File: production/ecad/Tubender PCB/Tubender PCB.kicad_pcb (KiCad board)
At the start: 2 copper layers, 210 parts, among them J10 640387-5, J11 640387-8, J12 640387-2, J13 640387-5, J14 640387-3, J15 640387-2, J16 640387-2, J17 640387-2, J18 640387-2, J19 640387-2, J2 640387-5, J20 640387-2, J21 640387-2, J22 640387-2, J23 640387-2, J24 640387-2, J25 640387-2, J26 640387-2, J27 640387-2, J28 640387-2, J29 1-640387-0, J3 640387-5, J30 640387-2, J31 640387-5, J32 USB4110GFA, J4 640387-5, J5 640387-6, J6 640387-6, J8 640387-6, J9 640387-5, Q1 AO3400A, Q2 AO3400A, U1 LMR36520FADDAR, U10 MCP23017-E_SO, U11 SN74AHC1G125DBVR, U12 LM5146RGYR, U13 LM5017SDX/NOPB, U2 ESP32-WROOM-32UE_M113EH6400UH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, U3 MCP23017-E_SO, U5 TPSM265R1V5SILR, U6 CP2102N-A02-GQFN28, U8 CD4051BE, U9 CD4051BE, Y1 ABM8-20.000MHz-10-B1U-T

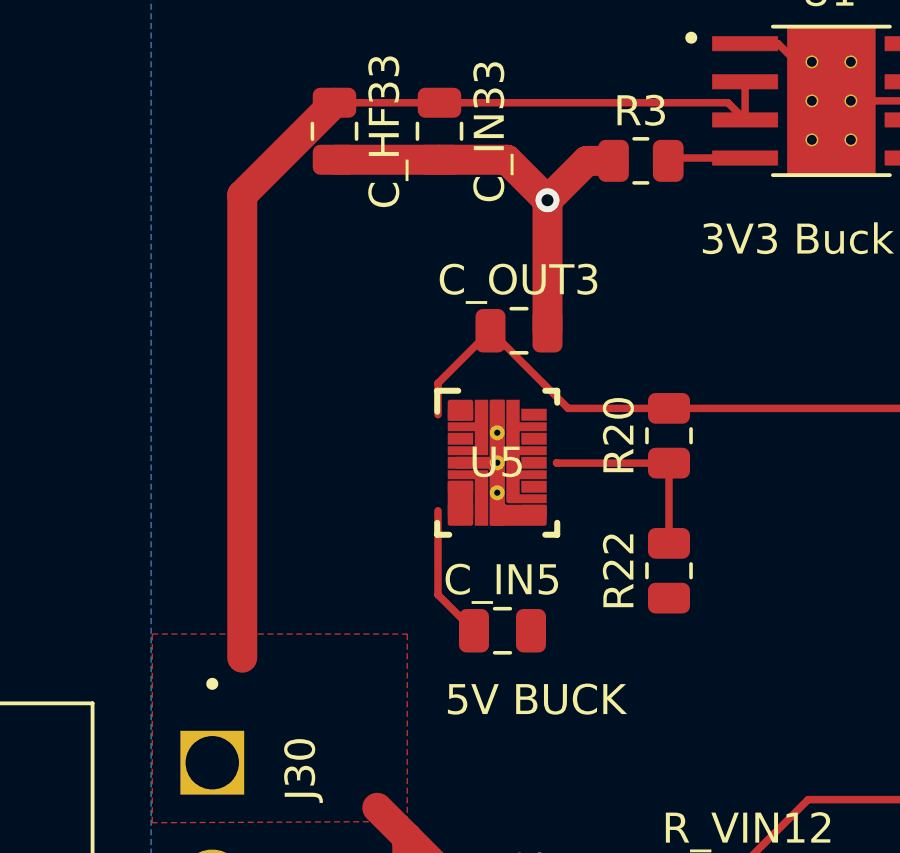
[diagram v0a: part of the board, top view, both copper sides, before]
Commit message: connected one line on 5V Buck
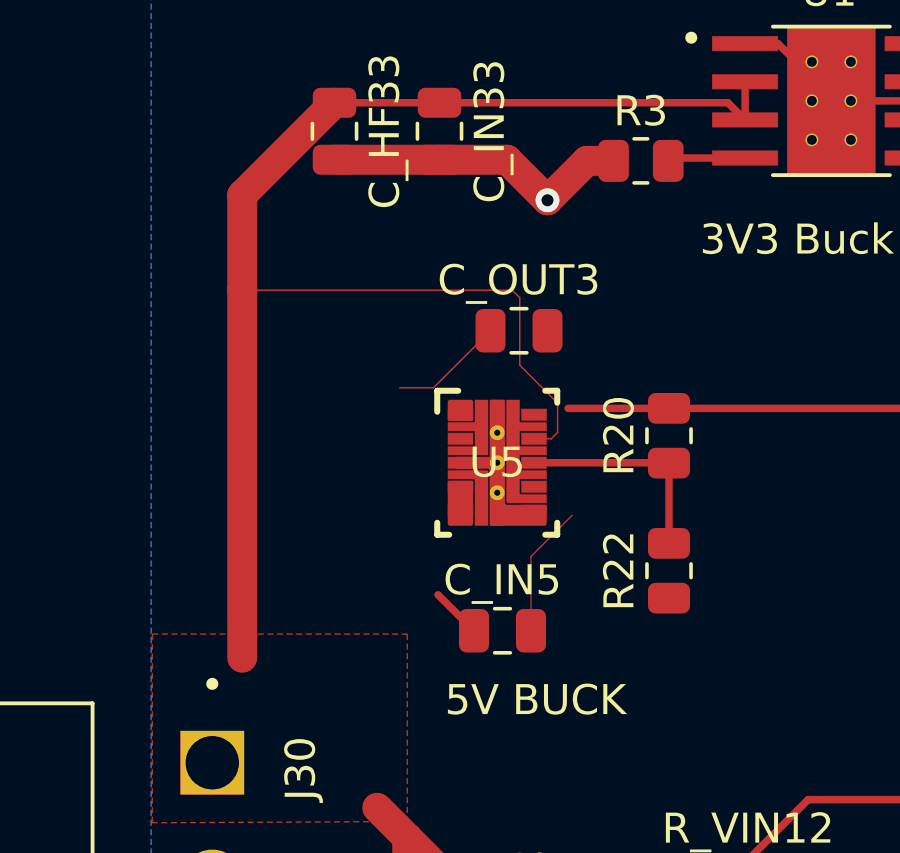
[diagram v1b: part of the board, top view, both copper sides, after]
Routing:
- net 48V: track 212.6 -> 225.1 mm
- net 5V: track 49.5 -> 46.1 mm
- net Net-(U5-SENSE+_FB): track 6.43 -> 7.18 mm
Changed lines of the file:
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@@
 		(tags "tdson ")
 		(property "Reference" "Q_HI1"
-			(at 0 -3.5 360)
+			(at 0 -3.5 0)
 			(layer "F.SilkS")
 			(effects
@@
 		)
 		(property "Value" "CSD19502Q5B"
-			(at 0 4.925 360)
+			(at 0 4.925 0)
 			(layer "F.Fab")
 			(effects
@@
 		)
 		(fp_text user "${REFERENCE}"
-			(at 0 0 360)
+			(at 0 0 0)
 			(layer "F.Fab")
 			(effects
@@
 		(tags "tdson ")
 		(property "Reference" "Q_LO1"
-			(at 0 -3.5 360)
+			(at 0 -3.5 0)
 			(layer "F.SilkS")
 			(effects
@@
 		)
 		(property "Value" "CSD19534Q5A"
-			(at 0 3.5 360)
+			(at 0 3.5 0)
 			(layer "F.Fab")
 			(effects
@@
 		)
 		(fp_text user "${REFERENCE}"
-			(at 0 0 360)
+			(at 0 0 0)
 			(layer "F.Fab")
 			(effects
@@
 	)
 	(segment
-		(start 74.174999 55.5)
-		(end 74.174999 59.849999)
-		(width 1)
+		(start 75.1425 84.8225)
+		(end 75.085 84.88)
+		(width 0.25)
 		(layer "F.Cu")
 		(net 2)
 	)
 	(segment
-		(start 75.1425 84.8225)
-		(end 75.085 84.88)
-		(width 0.25)
+		(start 73.624999 67.375001)
+		(end 75 66)
+		(width 0.001)
 		(layer "F.Cu")
 		(net 2)
@@
 	)
 	(segment
+		(start 73.624999 69.849999)
+		(end 73.624999 67.375001)
+		(width 0.001)
+		(layer "F.Cu")
+		(net 2)
+	)
+	(segment
 		(start 91.1575 99.13)
 		(end 92.975 99.13)
@@
 	)
 	(segment
-		(start 70.88 78.13)
-		(end 69.5 76.75)
-		(width 1)
+		(start 73.25 61)
+		(end 73.25 58.75)
+		(width 0.05)
 		(layer "F.Cu")
 		(net 34)
 	)
 	(segment
-		(start 64 55.325)
-		(end 64 70.75)
+		(start 70.88 78.13)
+		(end 69.5 76.75)
 		(width 1)
 		(layer "F.Cu")
@@
 	)
 	(segment
+		(start 74.299996 63.450004)
+		(end 74.512499 63.237501)
+		(width 0.05)
+		(layer "F.Cu")
+		(net 34)
+	)
+	(segment
 		(start 109.300305 102.199695)
 		(end 111.75 99.75)
@@
 	)
 	(segment
+		(start 73 58.5)
+		(end 64 58.5)
+		(width 0.05)
+		(layer "F.Cu")
+		(net 34)
+	)
+	(segment
 		(start 69.5 97.5)
 		(end 75.5 103.5)
@@
 	)
 	(segment
+		(start 64 58.5)
+		(end 64 70.75)
+		(width 1)
+		(layer "F.Cu")
+		(net 34)
+	)
+	(segment
+		(start 73.724999 63.450004)
+		(end 74.299996 63.450004)
+		(width 0.05)
+		(layer "F.Cu")
+		(net 34)
+	)
+	(segment
 		(start 69.5 76.75)
 		(end 69.5 97.5)
@@
 	)
 	(segment
-		(start 70.525001 68.650001)
-		(end 70.525001 65.849999)
-		(width 0.25)
-		(layer "F.Cu")
-		(net 34)
-	)
-	(segment
 		(start 71.724999 69.849999)
 		(end 70.525001 68.650001)
@@
 	)
 	(segment
+		(start 73.25 58.75)
+		(end 73 58.5)
+		(width 0.05)
+		(layer "F.Cu")
+		(net 34)
+	)
+	(segment
 		(start 109.300305 104.603591)
 		(end 109.300305 102.199695)
@@
 	)
 	(segment
+		(start 64 55.325)
+		(end 64 58.5)
+		(width 1)
+		(layer "F.Cu")
+		(net 34)
+	)
+	(segment
+		(start 74.512499 63.237501)
+		(end 74.512499 62.262499)
+		(width 0.05)
+		(layer "F.Cu")
+		(net 34)
+	)
+	(segment
 		(start 81.775 109.93)
 		(end 80.25 109.93)
@@
 	)
 	(segment
+		(start 74.512499 62.262499)
+		(end 73.25 61)
+		(width 0.05)
+		(layer "F.Cu")
+		(net 34)
+	)
+	(segment
 		(start 69.5 76.75)
 		(end 68.5 75.75)
@@
 	)
 	(segment
-		(start 70.525001 61.599997)
-		(end 70.525001 62.650001)
-		(width 0.25)
+		(start 70.374998 61.75)
+		(end 69.25 61.75)
+		(width 0.05)
 		(layer "F.Cu")
 		(net 38)
@@
 	)
 	(segment
-		(start 78.224999 62.437499)
-		(end 74.862499 62.437499)
-		(width 0.25)
-		(layer "F.Cu")
-		(net 38)
-	)
-	(segment
 		(start 72.274999 59.849999)
-		(end 70.525001 61.599997)
-		(width 0.25)
+		(end 70.374998 61.75)
+		(width 0.05)
 		(layer "F.Cu")
 		(net 38)
 	)
 	(segment
-		(start 74.862499 62.437499)
-		(end 72.274999 59.849999)
+		(start 78.224999 62.437499)
+		(end 74.862499 62.437499)
 		(width 0.25)
 		(layer "F.Cu")
@@
 	)
 	(segment
-		(start 78.224999 64.262499)
-		(end 74.487495 64.262499)
-		(width 0.25)
+		(start 78.212503 64.250003)
+		(end 78.224999 64.262499)
+		(width 0.05)
 		(layer "F.Cu")
 		(net 112)
 	)
 	(segment
-		(start 74.487495 64.262499)
-		(end 74.474999 64.250003)
+		(start 73.724999 64.250003)
+		(end 78.212503 64.250003)
 		(width 0.25)
 		(layer "F.Cu")

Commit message: starting to layout non-power stuff
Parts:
- removed U8, U9: CD4051BE, ${KIPRJMOD}:DIP794W45P254L1969H508Q16
- added C5: 0.1uF, Capacitor_SMD:C_0805_2012Metric, F.Cu at (-242.2, -243.4)
- added J35: 640387-3, ${KIPRJMOD}:TE_640387-3, F.Cu at (-126.7, -179.6)
- added J37: 640387-3, ${KIPRJMOD}:TE_640387-3, F.Cu at (-65.2, -179.6)
- added J8: 640387-3, ${KIPRJMOD}:TE_640387-3, F.Cu at (-96.0, -179.6)
- added J9: 640387-3, ${KIPRJMOD}:TE_640387-3, F.Cu at (-111.4, -179.6)
- added R17: 100k, Resistor_SMD:R_0805_2012Metric, F.Cu at (-242.2, -251.3)
- added R18: 10k, Resistor_SMD:R_0805_2012Metric, F.Cu at (-242.2, -248.4)
- added R43: 5.1K, Resistor_SMD:R_0805_2012Metric, F.Cu at (-237.8, -260.2)
- added R44: 5.1K, Resistor_SMD:R_0805_2012Metric, F.Cu at (-237.8, -257.2)
- added R45: 10k, Resistor_SMD:R_0805_2012Metric, F.Cu at (-237.8, -254.3)
- added R48: 0, Resistor_SMD:R_0805_2012Metric, F.Cu at (-237.8, -251.3)
- added R5: 10K, Resistor_SMD:R_0805_2012Metric, F.Cu at (-242.2, -240.4)
- added R6: 100k, Resistor_SMD:R_0805_2012Metric, F.Cu at (-242.2, -260.2)
- added R7: 100k, Resistor_SMD:R_0805_2012Metric, F.Cu at (-242.2, -257.2)
- added R71: 5.1K, Resistor_SMD:R_0805_2012Metric, F.Cu at (-237.8, -248.4)
- added R72: 15k, Resistor_SMD:R_0805_2012Metric, F.Cu at (-233.4, -260.2)
- added R73: 5.1K, Resistor_SMD:R_0805_2012Metric, F.Cu at (-233.4, -257.2)
- added R74: 15k, Resistor_SMD:R_0805_2012Metric, F.Cu at (-233.4, -254.3)
- added R75: 0, Resistor_SMD:R_0805_2012Metric, F.Cu at (-233.4, -251.3)
- added R8: 100k, Resistor_SMD:R_0805_2012Metric, F.Cu at (-242.2, -254.3)
- moved J16 511.2 mm to (-305.5, -110.9)
- moved J21 511.2 mm to (-305.5, -90.9)
- moved J26 511.2 mm to (-305.5, -71.0)
- moved J12 511.2 mm to (-325.6, -110.9)
- moved J15 511.2 mm to (-315.5, -110.9)
- moved J17 511.2 mm to (-295.4, -110.9)
- moved J18 511.2 mm to (-285.4, -110.9)
- moved J19 511.2 mm to (-325.6, -90.9)
- moved J20 511.2 mm to (-315.5, -90.9)
- moved J22 511.2 mm to (-295.4, -90.9)
- moved J23 511.2 mm to (-285.4, -90.9)
- moved J24 511.2 mm to (-325.6, -71.0)
- moved J25 511.2 mm to (-315.5, -71.0)
- moved J27 511.2 mm to (-295.4, -71.0)
- moved J28 511.2 mm to (-285.4, -71.0)
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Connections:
- J14 pad 1: 24V -> Net-(J14-Pad1)
- R_ILIM1 pad 1: Net-(Q_LO1-D) -> Net-(U12-ILIM)
- R_ILIM1 pad 2: Net-(U12-ILIM) -> Net-(Q_LO1-D)
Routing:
- net 7-SEG_SER: track 0.00 -> 95.0 mm
- net 7-SEG_OEb: track 0.00 -> 94.9 mm
- net 7-SEG_A0: track 0.00 -> 84.9 mm
- net 7-SEG_A1: track 0.00 -> 82.0 mm
- net 7-SEG_Gb: track 0.00 -> 79.0 mm
- net BENDING_L_ENA: track 0.00 -> 68.9 mm
- net 3.3V: track 31.6 -> 53.7 mm

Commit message: more changes
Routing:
- net 7-SEG_RCLK: track 0.00 -> 141.2 mm
- net 7-SEG_SRCLK: track 0.00 -> 107.6 mm
- net 7-SEG_OEb: track 94.9 -> 0.00 mm
- net 7-SEG_SER: track 95.0 -> 95.7 mm

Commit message: working on mcu layout
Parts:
- added IC1: 74HC4050D, ${KIPRJMOD}:SOT109-1_NXP, F.Cu at (176.1, 92.0)
- added IC2: RA8875L3N, ${KIPRJMOD}:QFP40P1600X1600X160-128N, F.Cu at (154.9, 93.6)
- added IC3: CD4051BM96, ${KIPRJMOD}:SOIC127P600X175-16N, F.Cu at (161.3, 126.8)
- added IC4: CD4051BM96, ${KIPRJMOD}:SOIC127P600X175-16N, F.Cu at (170.4, 126.8)
- added J1: 640387-2, ${KIPRJMOD}:TE_640387-2, F.Cu at (286.0, 53.0)
- added J10: 640387-2, ${KIPRJMOD}:TE_640387-2, F.Cu at (255.8, 53.0)
- added J33: 640387-2, ${KIPRJMOD}:TE_640387-2, F.Cu at (245.8, 53.0)
- added J34: 640387-2, ${KIPRJMOD}:TE_640387-2, F.Cu at (235.7, 53.0)
- added J5: 640387-2, ${KIPRJMOD}:TE_640387-2, F.Cu at (275.9, 53.0)
- added J6: 640387-2, ${KIPRJMOD}:TE_640387-2, F.Cu at (265.9, 53.0)
- added J7: 4-1734592-0, ${KIPRJMOD}:TE_4-1734592-0, F.Cu at (191.4, 81.2)
- added TP14: 5006, ${KIPRJMOD}:KEYSTONE_5006, F.Cu at (206.0, -89.7)
- added TP15: 5006, ${KIPRJMOD}:KEYSTONE_5006, F.Cu at (206.0, -85.0)
- added TP16: 5006, ${KIPRJMOD}:KEYSTONE_5006, F.Cu at (206.0, -80.2)
- added TP17: 5006, ${KIPRJMOD}:KEYSTONE_5006, F.Cu at (206.0, -75.5)
- added TP18: 5006, ${KIPRJMOD}:KEYSTONE_5006, F.Cu at (206.0, -70.8)
- added TP19: 5006, ${KIPRJMOD}:KEYSTONE_5006, F.Cu at (210.7, -89.7)
- added TP20: 5006, ${KIPRJMOD}:KEYSTONE_5006, F.Cu at (210.7, -85.0)
- added TP21: 5006, ${KIPRJMOD}:KEYSTONE_5006, F.Cu at (210.7, -80.2)
- added TP22: 5006, ${KIPRJMOD}:KEYSTONE_5006, F.Cu at (210.7, -75.5)
- added TP23: 5006, ${KIPRJMOD}:KEYSTONE_5006, F.Cu at (210.7, -70.8)
- added TP24: 5006, ${KIPRJMOD}:KEYSTONE_5006, F.Cu at (215.5, -89.7)
- added TP25: 5006, ${KIPRJMOD}:KEYSTONE_5006, F.Cu at (215.5, -85.0)
- added TP26: 5006, ${KIPRJMOD}:KEYSTONE_5006, F.Cu at (215.5, -80.2)
- added TP27: 5006, ${KIPRJMOD}:KEYSTONE_5006, F.Cu at (215.5, -75.5)
- moved J31 775.0 mm to (265.6, 199.5)
- moved R5 682.3 mm to (348.0, 101.9), turned to 90 degrees
- moved C5 681.2 mm to (345.0, 101.9), turned to 90 degrees
- moved R18 679.5 mm to (340.1, 101.9), turned to 90 degrees
- moved R17 678.5 mm to (337.1, 101.9), turned to 90 degrees
- moved R8 677.5 mm to (334.1, 101.9), turned to 90 degrees
- moved R7 676.6 mm to (331.2, 101.9), turned to 90 degrees
- moved R71 661.3 mm to (323.3, 101.7), turned to 90 degrees
- moved R48 660.4 mm to (320.4, 101.7), turned to 90 degrees
- moved R45 659.5 mm to (317.4, 101.7), turned to 90 degrees
- moved R44 658.6 mm to (314.4, 101.7), turned to 90 degrees
- moved R43 657.7 mm to (311.5, 101.7), turned to 90 degrees
- moved R6 653.7 mm to (283.2, 128.7), turned to 90 degrees
- moved R75 645.3 mm to (307.1, 101.2), turned to 90 degrees
- moved R74 644.4 mm to (304.1, 101.2), turned to 90 degrees
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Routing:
- net 3.3V: track 53.7 -> 117.4 mm
- net 7-SEG_A1: track 82.0 -> 102.9 mm
- net 7-SEG_Gb: track 79.0 -> 98.7 mm
- net 7-SEG_A0: track 84.9 -> 104.6 mm
- net 7-SEG_SER: track 95.7 -> 88.1 mm
- net 7-SEG_SRCLK: track 107.6 -> 100.3 mm
- net 7-SEG_RCLK: track 141.2 -> 135.7 mm
- net DIE_LIMIT_1: track 0.00 -> 4.01 mm
- net BENDING_L_ENA: track 68.9 -> 70.3 mm
- net ESP_SCK: track 0.00 -> 1.27 mm

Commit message: a few lines here and there
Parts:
- moved C27 314.9 mm to (82.8, 193.6), turned to 90 degrees
- moved R54 310.5 mm to (56.2, 195.0)
- moved C25 309.0 mm to (61.5, 196.8)
- moved C28 306.2 mm to (104.8, 193.5), turned to 90 degrees
- moved C24 305.4 mm to (60.1, 189.4)
- moved R59 304.0 mm to (111.6, 192.2), turned to -90 degrees
- moved J18 303.1 mm to (52.6, 185.6), turned to -90 degrees
- moved R55 301.5 mm to (67.7, 192.2), turned to -90 degrees
- moved R53 301.4 mm to (62.2, 184.5), turned to 180 degrees
- moved C29 301.0 mm to (115.8, 193.6), turned to 90 degrees
- moved C26 299.7 mm to (71.7, 193.6), turned to 90 degrees
- moved R60 299.5 mm to (122.5, 192.2), turned to -90 degrees
- moved C23 298.9 mm to (60.1, 179.4)
- moved C30 296.1 mm to (127.0, 193.6), turned to 90 degrees
- moved R56 295.6 mm to (78.8, 192.2), turned to -90 degrees
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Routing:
- net 7-SEG_RCLK: track 135.7 -> 0.00 mm
- net 7-SEG_A0: track 104.6 -> 0.00 mm
- net 7-SEG_A1: track 102.9 -> 1.35 mm
- net 7-SEG_SRCLK: track 100.3 -> 0.00 mm
- net 7-SEG_Gb: track 98.7 -> 0.00 mm
- net 7-SEG_SER: track 88.1 -> 0.00 mm
- net BENDING_L_ENA: track 70.3 -> 0.00 mm
- net BUTTON_13: track 0.00 -> 12.5 mm
- net BUTTON_9: track 0.00 -> 12.5 mm
- net BUTTON_10: track 0.00 -> 12.4 mm
- net BUTTON_12: track 0.00 -> 12.4 mm
- net BUTTON_11: track 0.00 -> 12.4 mm
- net BUTTON_1: track 0.00 -> 11.3 mm
- net BUTTON_2: track 0.00 -> 11.0 mm
- net BUTTON_8: track 0.00 -> 10.9 mm
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
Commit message: added some traces
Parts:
- moved IC3 86.3 mm to (287.8, 145.2), turned to 180 degrees
- moved IC4 75.1 mm to (287.8, 130.9), turned to 180 degrees
- moved R6 0.25 mm to (267.2, 125.2)
- turned C3 to 90 degrees
- turned C4 to 90 degrees
- turned U2 to 90 degrees
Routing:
- net BUTTON_0: track 10.5 -> 432.9 mm, vias 0 -> 2
- net BUTTON_13: track 12.5 -> 358.2 mm, vias 0 -> 2
- net BUTTON_3: track 7.75 -> 326.9 mm, vias 0 -> 2
- net BUTTON_12: track 12.4 -> 287.2 mm, vias 0 -> 2
- net BUTTON_14: track 10.5 -> 208.2 mm, vias 0 -> 2
- net DIE_CLAMP_DIR+: track 0.00 -> 176.3 mm
- net DIE_CLAMP_PUL+: track 0.00 -> 166.5 mm
- net DIE_CLAMP_ENA+: track 0.00 -> 150.8 mm
- net ADVANCING_DIR+: track 0.00 -> 133.3 mm
- net ADVANCING_ENA+: track 0.00 -> 128.1 mm
- net ROTATION_PUL+: track 0.00 -> 115.8 mm
- net ROTATION_DIR+: track 0.00 -> 115.6 mm
- net ROTATION_ENA+: track 0.00 -> 111.6 mm
- net BUTTON_2: track 11.0 -> 114.4 mm, vias 0 -> 2
- net CHUCK_CLAMP_PUL+: track 0.00 -> 83.7 mm
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
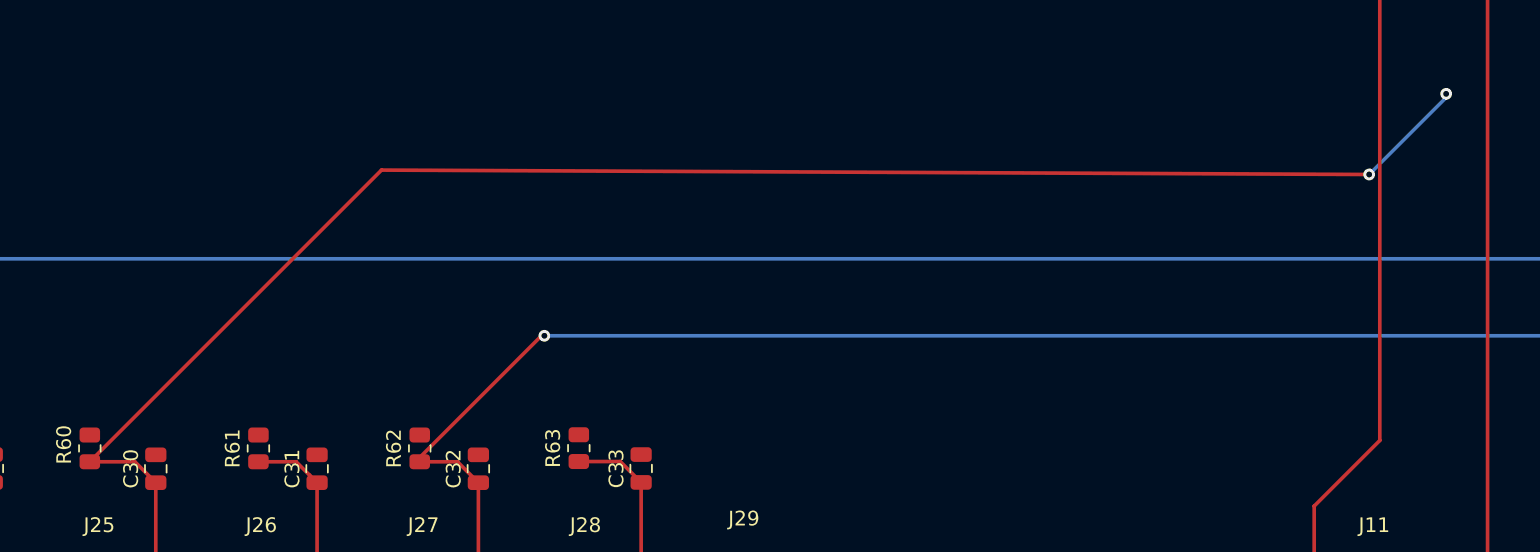
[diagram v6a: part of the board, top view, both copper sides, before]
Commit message: small change, removed one trace
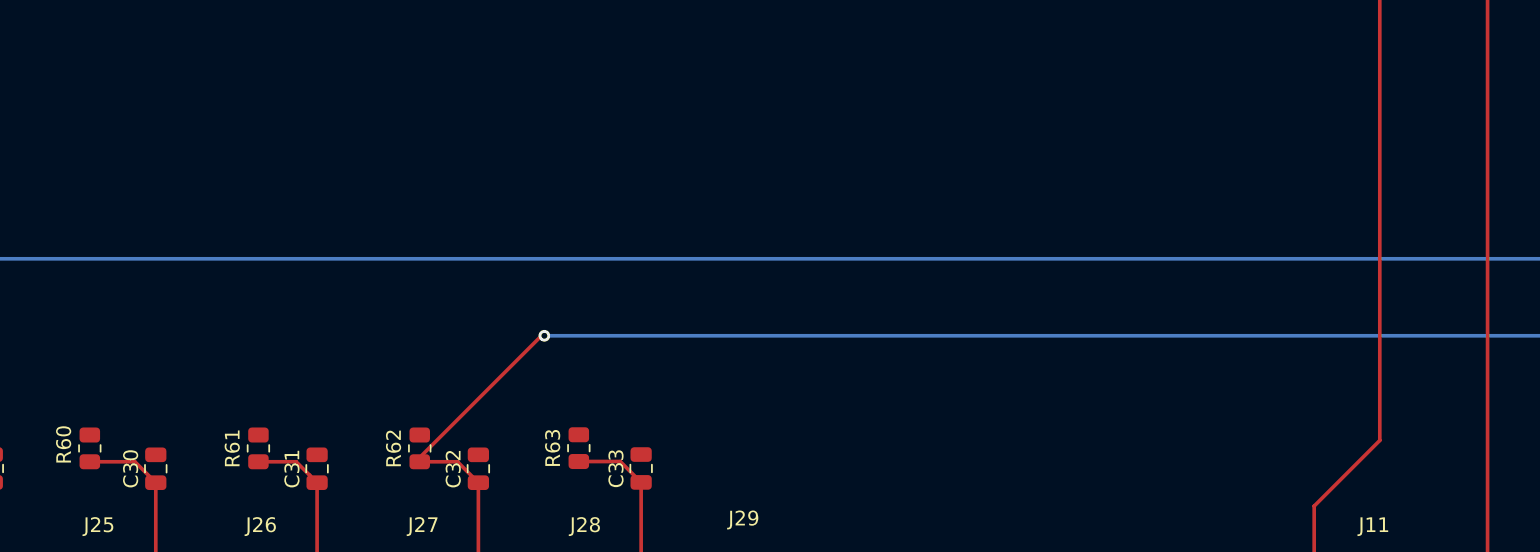
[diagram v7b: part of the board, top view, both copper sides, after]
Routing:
- net BUTTON_2: track 114.4 -> 11.0 mm, vias 2 -> 0
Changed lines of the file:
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@@
 		(at 287.775 145.175 180)
 		(property "Reference" "IC3"
-			(at -0.795 -6.035 360)
+			(at -0.795 -6.035 0)
 			(layer "F.SilkS")
 			(effects
@@
 		)
 		(property "Value" "CD4051BM96"
-			(at 8.095 6.035 360)
+			(at 8.095 6.035 0)
 			(layer "F.Fab")
 			(effects
@@
 		)
 		(property "Footprint" "${KIPRJMOD}:SOIC127P600X175-16N"
-			(at 0 0 360)
+			(at 0 0 0)
 			(layer "F.Fab")
 			(hide yes)
@@
 		)
 		(property "Datasheet" "http://www.ti.com/general/docs/lit/getliterature.tsp?genericPartNumber=CD4051B&&fileType=pdf"
-			(at 0 0 360)
+			(at 0 0 0)
 			(layer "F.Fab")
 			(hide yes)
@@
 		)
 		(property "Description" "CMOS 8-Ch Analog Mux/Demux CD4051BM96G4 CD4051BM96, Multiplexer/Demultiplexer Single 8:1, 12 V, 15 V, 18 V, 5 V, 9 V, 16-Pin, SOIC, 1"
-			(at 0 0 360)
+			(at 0 0 0)
 			(layer "F.Fab")
 			(hide yes)
@@
 		(at 287.775 130.895 180)
 		(property "Reference" "IC4"
-			(at -0.795 -6.035 360)
+			(at -0.795 -6.035 0)
 			(layer "F.SilkS")
 			(effects
@@
 		)
 		(property "Value" "CD4051BM96"
-			(at 8.095 6.035 360)
+			(at 8.095 6.035 0)
 			(layer "F.Fab")
 			(effects
@@
 		)
 		(property "Footprint" "${KIPRJMOD}:SOIC127P600X175-16N"
-			(at 0 0 360)
+			(at 0 0 0)
 			(layer "F.Fab")
 			(hide yes)
@@
 		)
 		(property "Datasheet" "http://www.ti.com/general/docs/lit/getliterature.tsp?genericPartNumber=CD4051B&&fileType=pdf"
-			(at 0 0 360)
+			(at 0 0 0)
 			(layer "F.Fab")
 			(hide yes)
@@
 		)
 		(property "Description" "CMOS 8-Ch Analog Mux/Demux CD4051BM96G4 CD4051BM96, Multiplexer/Demultiplexer Single 8:1, 12 V, 15 V, 18 V, 5 V, 9 V, 16-Pin, SOIC, 1"
-			(at 0 0 360)
+			(at 0 0 0)
 			(layer "F.Fab")
 			(hide yes)
@@
 	)
 	(segment
-		(start 209.75 173.5)
-		(end 142.3925 173.2)
-		(width 0.25)
-		(layer "F.Cu")
-		(net 20)
-	)
-	(segment
-		(start 215 168)
-		(end 215 168)
-		(width 0.25)
-		(layer "F.Cu")
-		(net 20)
-	)
-	(segment
 		(start 122.5 193.0925)
 		(end 125.575 193.0925)
@@
 	)
 	(segment
-		(start 142.3925 173.2)
-		(end 122.5 193.0925)
-		(width 0.25)
-		(layer "F.Cu")
-		(net 20)
-	)
-	(segment
 		(start 125.575 193.0925)
 		(end 127 194.5175)
@@
 	)
 	(segment
-		(start 209.8 173.2)
-		(end 209.75 173.5)
-		(width 0.25)
-		(layer "F.Cu")
-		(net 20)
-	)
-	(segment
 		(start 127 200.28312)
 		(end 126.91312 200.37)
@@
 		(net 20)
 	)
-	(via
-		(at 209.75 173.5)
-		(size 0.8)
-		(drill 0.4)
-		(layers "F.Cu" "B.Cu")
-		(net 20)
-	)
-	(via
-		(at 215 168)
-		(size 0.8)
-		(drill 0.4)
-		(layers "F.Cu" "B.Cu")
-		(net 20)
-	)
-	(segment
-		(start 209.75 173.5)
-		(end 215 168.25)
-		(width 0.25)
-		(layer "B.Cu")
-		(net 20)
-	)
-	(segment
-		(start 215 168.25)
-		(end 215 168)
-		(width 0.25)
-		(layer "B.Cu")
-		(net 20)
-	)
